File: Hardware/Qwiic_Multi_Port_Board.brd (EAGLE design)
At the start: 25.4 x 25.4 mm, 26 parts, among them J1 QWIIC_RIGHT_ANGLE, J2 QWIIC_RIGHT_ANGLE, J3 QWIIC_RIGHT_ANGLE, J4 QWIIC_RIGHT_ANGLE

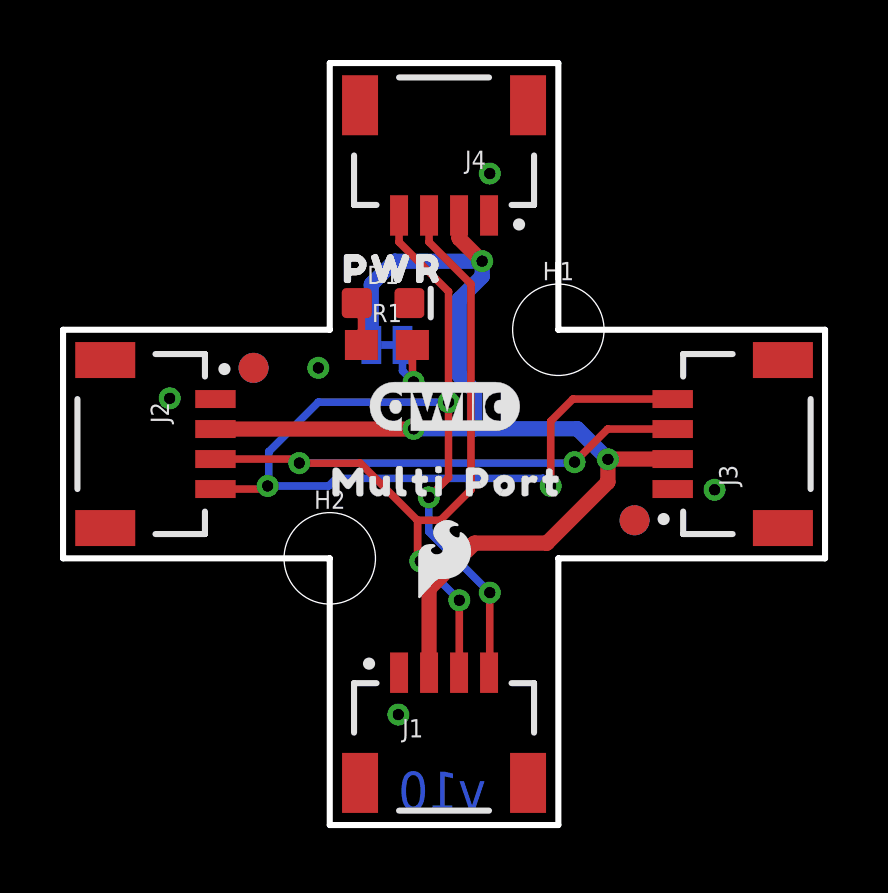
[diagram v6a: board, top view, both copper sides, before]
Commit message: Created star-shaped Qwiic Ninja Star and updated Multi Port
Updated Qwiic Multi Port with QC Double check concerns:
Removed wire stub
Approve DRC errors
Move via to not clip the t in "Port" on top
Moved power jumper and silk so that jumper silk and SF logo don't overlap
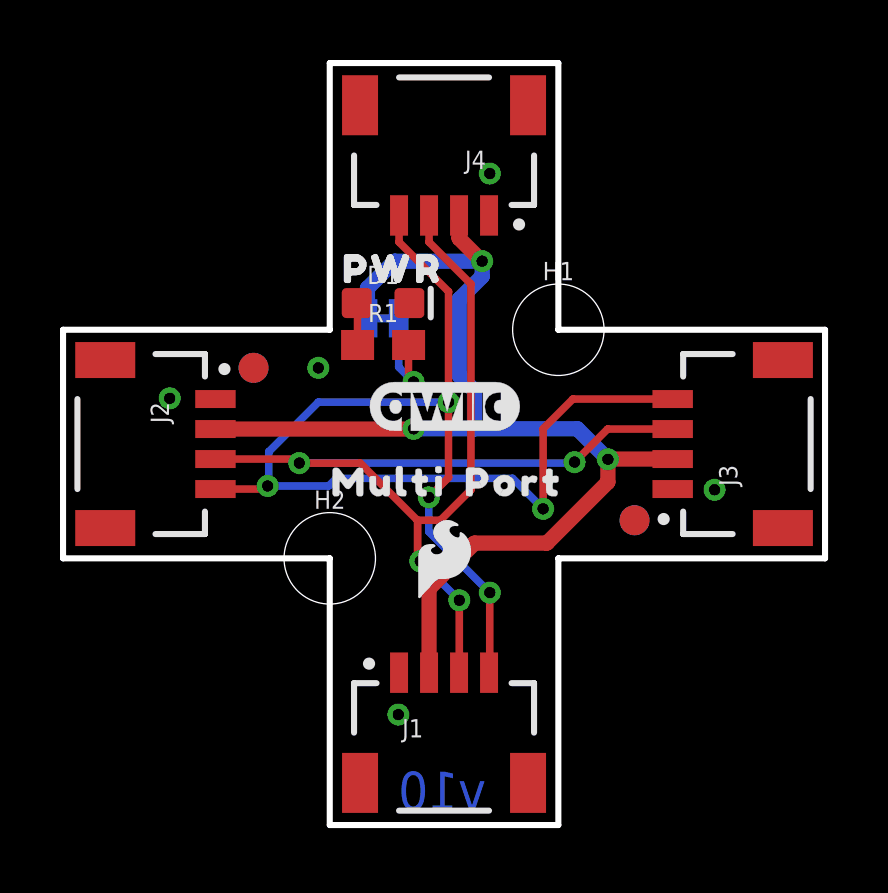
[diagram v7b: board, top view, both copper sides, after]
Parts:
- moved JP1 0.90 mm to (10.7, 16.9)
- moved U$3 0.76 mm to (13.0, 18.5)
- moved R1 0.13 mm to (10.7, 16.0)
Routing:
- net N$2: track 2.63 -> 3.63 mm
- net SCL: track 42.8 -> 43.8 mm
- net 3.3V: track 40.7 -> 39.8 mm
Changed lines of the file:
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@@
 <drawing>
 <settings>
-<setting alwaysvectorfont="no"/>
+<setting alwaysvectorfont="yes"/>
 <setting verticaltext="up"/>
 </settings>
@@
 <layer number="45" name="Holes" color="7" fill="1" visible="yes" active="yes"/>
 <layer number="46" name="Milling" color="3" fill="1" visible="no" active="yes"/>
-<layer number="47" name="Measures" color="7" fill="1" visible="yes" active="yes"/>
+<layer number="47" name="Measures" color="7" fill="1" visible="no" active="yes"/>
 <layer number="48" name="Document" color="7" fill="1" visible="no" active="yes"/>
 <layer number="49" name="Reference" color="7" fill="1" visible="no" active="yes"/>
@@
 <attribute name="VALUE" x="10.668" y="16.764" size="0.6096" layer="27" font="vector" ratio="20" align="top-center"/>
 </element>
-<element name="R1" library="SparkFun-Resistors" package="0603" value="1k" x="10.795" y="16.002" smashed="yes">
-<attribute name="NAME" x="10.795" y="16.764" size="0.6096" layer="25" font="vector" ratio="20" align="bottom-center"/>
-<attribute name="PROD_ID" value="RES-07856" x="10.795" y="16.002" size="1.778" layer="27" font="vector" ratio="15" display="off"/>
-<attribute name="VALUE" x="10.795" y="15.24" size="0.6096" layer="27" font="vector" ratio="20" align="top-center"/>
+<element name="R1" library="SparkFun-Resistors" package="0603" value="1k" x="10.668" y="16.002" smashed="yes">
+<attribute name="NAME" x="10.668" y="16.764" size="0.6096" layer="25" font="vector" ratio="20" align="bottom-center"/>
+<attribute name="PROD_ID" value="RES-07856" x="10.668" y="16.002" size="1.778" layer="27" font="vector" ratio="15" display="off"/>
+<attribute name="VALUE" x="10.668" y="15.24" size="0.6096" layer="27" font="vector" ratio="20" align="top-center"/>
 </element>
 <element name="U$2" library="SparkFun-Aesthetics" package="SFE_LOGO_FLAME_.1" value="" x="12.7" y="8.89" smashed="yes"/>
@@
 <element name="FD3" library="SparkFun-Aesthetics" package="FIDUCIAL-1X2" value="FIDUCIAL1X2" x="19.05" y="10.16" smashed="yes"/>
 <element name="FD4" library="SparkFun-Aesthetics" package="FIDUCIAL-1X2" value="FIDUCIAL1X2" x="19.05" y="10.16" smashed="yes" rot="MR0"/>
-<element name="JP1" library="SparkFun-Jumpers" package="SMT-JUMPER_2_NC_TRACE_SILK" package3d_urn="urn:adsk.eagle:package:39281/1" value="PWR_LED" x="10.795" y="16.002" smashed="yes" rot="MR0">
-<attribute name="NAME" x="10.795" y="17.145" size="0.6096" layer="26" font="vector" ratio="20" rot="MR0" align="bottom-center"/>
-<attribute name="VALUE" x="10.795" y="14.859" size="0.6096" layer="28" font="vector" ratio="20" rot="MR0" align="top-center"/>
+<element name="JP1" library="SparkFun-Jumpers" package="SMT-JUMPER_2_NC_TRACE_SILK" package3d_urn="urn:adsk.eagle:package:39281/1" value="PWR_LED" x="10.668" y="16.891" smashed="yes" rot="MR0">
+<attribute name="NAME" x="10.668" y="18.034" size="0.6096" layer="26" font="vector" ratio="20" rot="MR0" align="bottom-center"/>
+<attribute name="VALUE" x="10.668" y="15.748" size="0.6096" layer="28" font="vector" ratio="20" rot="MR0" align="top-center"/>
 </element>
 <element name="LOGO1" library="SparkFun-Aesthetics" package="QWIIC_5MM" value="QWIIC_LOGO_5MM" x="12.7" y="13.97" smashed="yes"/>
@@
 <element name="LOGO4" library="SparkFun-Aesthetics" package="SFE_LOGO_NAME_.2" value="SFE_LOGO_NAME.2_INCH" x="12.7" y="12.7" smashed="yes" rot="MR0"/>
 <element name="U$1" library="output" package="PWR0" value="" x="8.636" y="18.542" smashed="yes"/>
-<element name="U$3" library="output" package="PWR0" value="" x="12.954" y="17.78" smashed="yes" rot="MR0"/>
+<element name="U$3" library="output" package="PWR0" value="" x="12.954" y="18.542" smashed="yes" rot="MR0"/>
 </elements>
 <signals>
@@
 <contactref element="J3" pad="4"/>
 <via x="6.8199" y="11.303" extent="1-16" drill="0.381"/>
-<via x="16.256" y="11.303" extent="1-16" drill="0.381"/>
-<wire x1="16.256" y1="13.462" x2="16.256" y2="11.303" width="0.254" layer="1"/>
+<via x="16.002" y="10.541" extent="1-16" drill="0.381"/>
+<wire x1="16.002" y1="13.208" x2="16.002" y2="10.541" width="0.254" layer="1"/>
 <wire x1="11.2" y1="20.32" x2="11.2" y2="19.431" width="0.254" layer="1"/>
 <wire x1="12.851" y1="17.78" x2="11.2" y2="19.431" width="0.254" layer="1"/>
@@
 <wire x1="6.7169" y1="11.2" x2="6.8199" y2="11.303" width="0.254" layer="1"/>
 <wire x1="20.32" y1="14.2" x2="16.994" y2="14.2" width="0.254" layer="1"/>
-<wire x1="16.994" y1="14.2" x2="16.256" y2="13.462" width="0.254" layer="1"/>
-<wire x1="16.256" y1="11.303" x2="16.002" y2="11.557" width="0.254" layer="16"/>
-<wire x1="16.002" y1="11.557" x2="9.1059" y2="11.557" width="0.254" layer="16"/>
+<wire x1="16.994" y1="14.2" x2="16.002" y2="13.208" width="0.254" layer="1"/>
+<wire x1="16.002" y1="10.541" x2="14.986" y2="11.557" width="0.254" layer="16"/>
+<wire x1="14.986" y1="11.557" x2="9.1059" y2="11.557" width="0.254" layer="16"/>
 <wire x1="9.1059" y1="11.557" x2="8.8519" y2="11.303" width="0.254" layer="16"/>
 <wire x1="8.8519" y1="11.303" x2="6.8199" y2="11.303" width="0.254" layer="16"/>
@@
 <wire x1="12.2" y1="5.08" x2="12.2" y2="7.882" width="0.508" layer="1"/>
 <wire x1="12.2" y1="7.882" x2="13.716" y2="9.398" width="0.508" layer="1"/>
-<wire x1="11.645" y1="13.247" x2="11.684" y2="13.208" width="0.508" layer="1"/>
 <contactref element="JP1" pad="2"/>
 <wire x1="13.2" y1="19.558" x2="13.962" y2="18.796" width="0.508" layer="1"/>
@@
 <via x="13.97" y="18.796" extent="1-16" drill="0.381"/>
 <wire x1="13.97" y1="18.796" x2="11.049" y2="18.796" width="0.508" layer="16"/>
-<wire x1="11.049" y1="18.796" x2="10.3505" y2="18.0975" width="0.508" layer="16"/>
+<wire x1="11.049" y1="18.796" x2="10.1473" y2="17.8943" width="0.508" layer="16"/>
 <wire x1="13.97" y1="18.796" x2="13.97" y2="18.288" width="0.508" layer="16"/>
 <wire x1="13.97" y1="18.288" x2="13.208" y2="17.526" width="0.508" layer="16"/>
@@
 <wire x1="13.716" y1="14.478" x2="13.716" y2="13.208" width="0.508" layer="16"/>
 <wire x1="13.208" y1="17.526" x2="13.208" y2="14.986" width="0.508" layer="16"/>
-<wire x1="10.2743" y1="16.002" x2="10.2743" y2="18.0213" width="0.508" layer="16"/>
-<wire x1="10.2743" y1="18.0213" x2="10.3505" y2="18.0975" width="0.508" layer="16"/>
+<wire x1="10.1473" y1="16.891" x2="10.1473" y2="17.8943" width="0.508" layer="16"/>
 </signal>
 <signal name="N$1">
 <contactref element="D1" pad="A"/>
 <contactref element="R1" pad="1"/>
-<wire x1="9.791" y1="17.399" x2="9.945" y2="17.245" width="0.254" layer="1"/>
-<wire x1="9.945" y1="17.245" x2="9.945" y2="16.002" width="0.254" layer="1"/>
+<wire x1="9.791" y1="17.399" x2="9.818" y2="17.372" width="0.254" layer="1"/>
+<wire x1="9.818" y1="17.372" x2="9.818" y2="16.002" width="0.254" layer="1"/>
 </signal>
 <signal name="N$2">
 <contactref element="R1" pad="2"/>
 <contactref element="JP1" pad="1"/>
-<wire x1="11.645" y1="16.002" x2="11.645" y2="14.8091" width="0.254" layer="1"/>
-<wire x1="11.645" y1="14.8091" x2="11.684" y2="14.7701" width="0.254" layer="1"/>
+<wire x1="11.518" y1="16.002" x2="11.518" y2="14.9361" width="0.254" layer="1"/>
+<wire x1="11.518" y1="14.9361" x2="11.684" y2="14.7701" width="0.254" layer="1"/>
 <via x="11.684" y="14.7701" extent="1-16" drill="0.381"/>
-<wire x1="11.684" y1="14.7701" x2="11.3157" y2="15.1384" width="0.254" layer="16"/>
-<wire x1="11.3157" y1="15.1384" x2="11.3157" y2="16.002" width="0.254" layer="16"/>
+<wire x1="11.684" y1="14.7701" x2="11.1887" y2="15.2654" width="0.254" layer="16"/>
+<wire x1="11.1887" y1="15.2654" x2="11.1887" y2="16.891" width="0.254" layer="16"/>
 </signal>
 </signals>
@@
 <mfgpreviewcolor name="substratecolor" color="0xFF786E46"/>
 </mfgpreviewcolors>
+<errors>
+</errors>
 </board>
 </drawing>

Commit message: Panelized
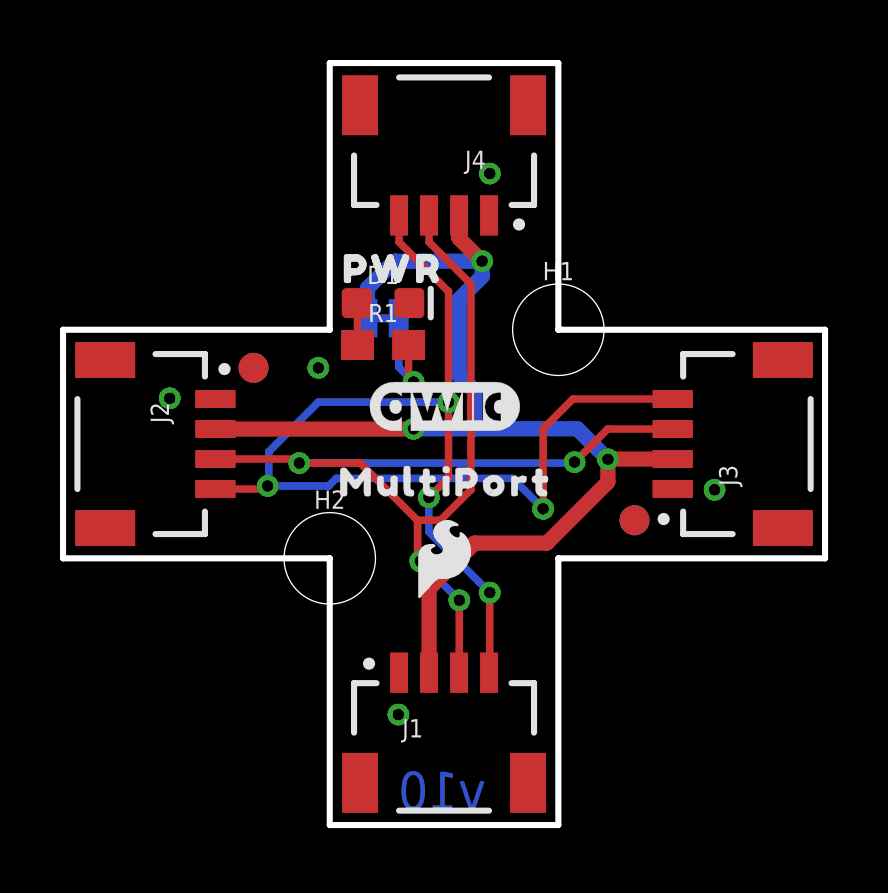
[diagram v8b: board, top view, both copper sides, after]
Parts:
- removed U$10: (no value), output:MULTI0
- removed U$12: (no value), output:PORT0
- added U$4: (no value), output:MULTIPORT0
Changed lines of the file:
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@@
 <?xml version="1.0" encoding="utf-8"?>
 <!DOCTYPE eagle SYSTEM "eagle.dtd">
-<eagle version="9.5.2">
+<eagle version="9.6.2">
 <drawing>
 <settings>
@@
 <layer number="23" name="tOrigins" color="15" fill="1" visible="yes" active="yes"/>
 <layer number="24" name="bOrigins" color="15" fill="1" visible="yes" active="yes"/>
-<layer number="25" name="tNames" color="7" fill="1" visible="no" active="yes"/>
-<layer number="26" name="bNames" color="7" fill="1" visible="no" active="yes"/>
-<layer number="27" name="tValues" color="7" fill="1" visible="no" active="yes"/>
-<layer number="28" name="bValues" color="7" fill="1" visible="no" active="yes"/>
-<layer number="29" name="tStop" color="7" fill="3" visible="no" active="yes"/>
-<layer number="30" name="bStop" color="7" fill="6" visible="no" active="yes"/>
-<layer number="31" name="tCream" color="7" fill="4" visible="no" active="yes"/>
-<layer number="32" name="bCream" color="7" fill="5" visible="no" active="yes"/>
-<layer number="33" name="tFinish" color="6" fill="3" visible="no" active="yes"/>
-<layer number="34" name="bFinish" color="6" fill="6" visible="no" active="yes"/>
-<layer number="35" name="tGlue" color="7" fill="4" visible="no" active="yes"/>
-<layer number="36" name="bGlue" color="7" fill="5" visible="no" active="yes"/>
-<layer number="37" name="tTest" color="7" fill="1" visible="no" active="yes"/>
-<layer number="38" name="bTest" color="7" fill="1" visible="no" active="yes"/>
-<layer number="39" name="tKeepout" color="4" fill="11" visible="no" active="yes"/>
-<layer number="40" name="bKeepout" color="1" fill="11" visible="no" active="yes"/>
-<layer number="41" name="tRestrict" color="4" fill="10" visible="no" active="yes"/>
-<layer number="42" name="bRestrict" color="1" fill="10" visible="no" active="yes"/>
-<layer number="43" name="vRestrict" color="2" fill="10" visible="no" active="yes"/>
-<layer number="44" name="Drills" color="7" fill="1" visible="no" active="yes"/>
+<layer number="25" name="tNames" color="7" fill="1" visible="yes" active="yes"/>
+<layer number="26" name="bNames" color="7" fill="1" visible="yes" active="yes"/>
+<layer number="27" name="tValues" color="7" fill="1" visible="yes" active="yes"/>
+<layer number="28" name="bValues" color="7" fill="1" visible="yes" active="yes"/>
+<layer number="29" name="tStop" color="7" fill="3" visible="yes" active="yes"/>
+<layer number="30" name="bStop" color="7" fill="6" visible="yes" active="yes"/>
+<layer number="31" name="tCream" color="7" fill="4" visible="yes" active="yes"/>
+<layer number="32" name="bCream" color="7" fill="5" visible="yes" active="yes"/>
+<layer number="33" name="tFinish" color="6" fill="3" visible="yes" active="yes"/>
+<layer number="34" name="bFinish" color="6" fill="6" visible="yes" active="yes"/>
+<layer number="35" name="tGlue" color="7" fill="4" visible="yes" active="yes"/>
+<layer number="36" name="bGlue" color="7" fill="5" visible="yes" active="yes"/>
+<layer number="37" name="tTest" color="7" fill="1" visible="yes" active="yes"/>
+<layer number="38" name="bTest" color="7" fill="1" visible="yes" active="yes"/>
+<layer number="39" name="tKeepout" color="4" fill="11" visible="yes" active="yes"/>
+<layer number="40" name="bKeepout" color="1" fill="11" visible="yes" active="yes"/>
+<layer number="41" name="tRestrict" color="4" fill="10" visible="yes" active="yes"/>
+<layer number="42" name="bRestrict" color="1" fill="10" visible="yes" active="yes"/>
+<layer number="43" name="vRestrict" color="2" fill="10" visible="yes" active="yes"/>
+<layer number="44" name="Drills" color="7" fill="1" visible="yes" active="yes"/>
 <layer number="45" name="Holes" color="7" fill="1" visible="yes" active="yes"/>
-<layer number="46" name="Milling" color="3" fill="1" visible="no" active="yes"/>
-<layer number="47" name="Measures" color="7" fill="1" visible="no" active="yes"/>
-<layer number="48" name="Document" color="7" fill="1" visible="no" active="yes"/>
-<layer number="49" name="Reference" color="7" fill="1" visible="no" active="yes"/>
+<layer number="46" name="Milling" color="3" fill="1" visible="yes" active="yes"/>
+<layer number="47" name="Measures" color="7" fill="1" visible="yes" active="yes"/>
+<layer number="48" name="Document" color="7" fill="1" visible="yes" active="yes"/>
+<layer number="49" name="Reference" color="7" fill="1" visible="yes" active="yes"/>
 <layer number="50" name="dxf" color="7" fill="1" visible="no" active="no"/>
 <layer number="51" name="tDocu" color="6" fill="1" visible="yes" active="yes"/>
-<layer number="52" name="bDocu" color="7" fill="1" visible="no" active="yes"/>
+<layer number="52" name="bDocu" color="7" fill="1" visible="yes" active="yes"/>
 <layer number="53" name="tGND_GNDA" color="7" fill="9" visible="no" active="no"/>
 <layer number="54" name="bGND_GNDA" color="1" fill="9" visible="no" active="no"/>
@@
 <element name="U$2" library="SparkFun-Aesthetics" package="SFE_LOGO_FLAME_.1" value="" x="12.7" y="8.89" smashed="yes"/>
 <element name="U$9" library="output" package="PWR0" value="" x="8.636" y="18.542" smashed="yes"/>
-<element name="U$10" library="output" package="MULTI0" value="" x="8.255" y="11.43" smashed="yes"/>
 <element name="U$11" library="output" package="MULTI0" value="" x="15.24" y="4.191" smashed="yes" rot="MR0"/>
-<element name="U$12" library="output" package="PORT0" value="" x="12.7" y="11.43" smashed="yes"/>
 <element name="U$13" library="output" package="PORT0" value="" x="14.986" y="2.794" smashed="yes" rot="MR0"/>
 <element name="FD1" library="SparkFun-Aesthetics" package="FIDUCIAL-1X2" value="FIDUCIAL1X2" x="6.35" y="15.24" smashed="yes" rot="MR0"/>
@@
 <element name="U$1" library="output" package="PWR0" value="" x="8.636" y="18.542" smashed="yes"/>
 <element name="U$3" library="output" package="PWR0" value="" x="12.954" y="18.542" smashed="yes" rot="MR0"/>
+<element name="U$4" library="output" package="MULTIPORT0" value="" x="8.509" y="11.43" smashed="yes"/>
 </elements>
 <signals>
